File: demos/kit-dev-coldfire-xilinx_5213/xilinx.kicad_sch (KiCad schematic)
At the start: 21 parts, among them P301 CONN_6, P302 CONN_2X2, P303 CONN_20X2, U301 XCR3256-TQ144

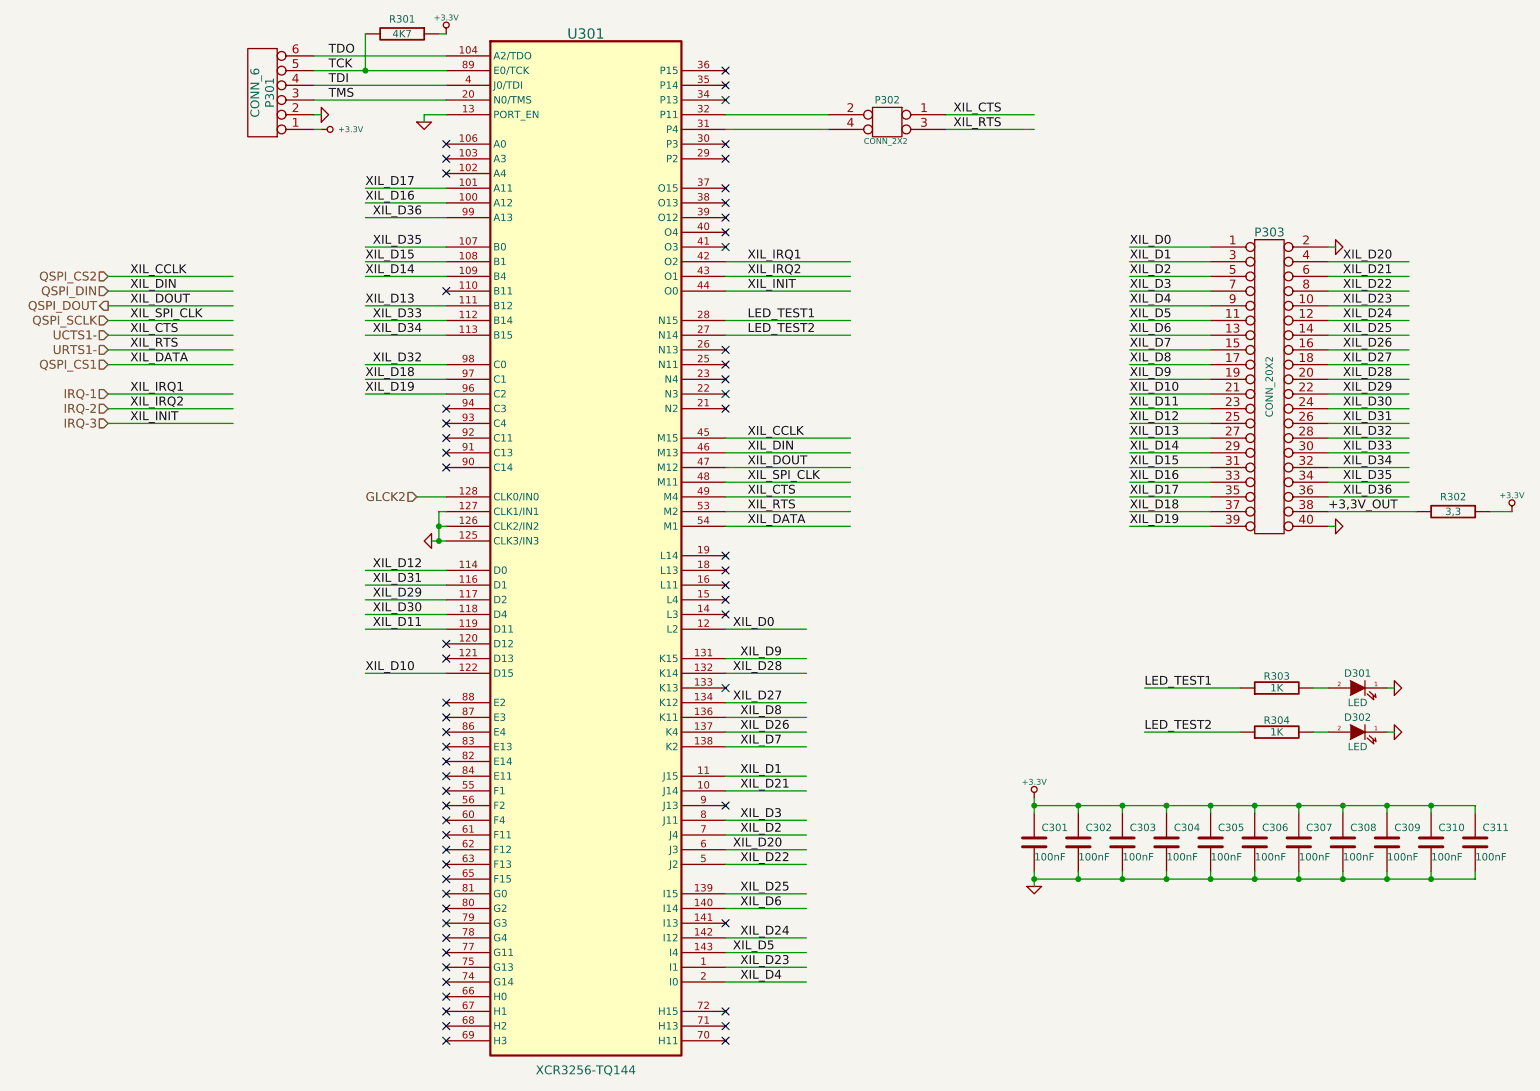
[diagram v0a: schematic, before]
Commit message: feat: update kicad to 9.0.0+dfsg-1
Signed-off-by: lhdjply <lhdjply@126.com>
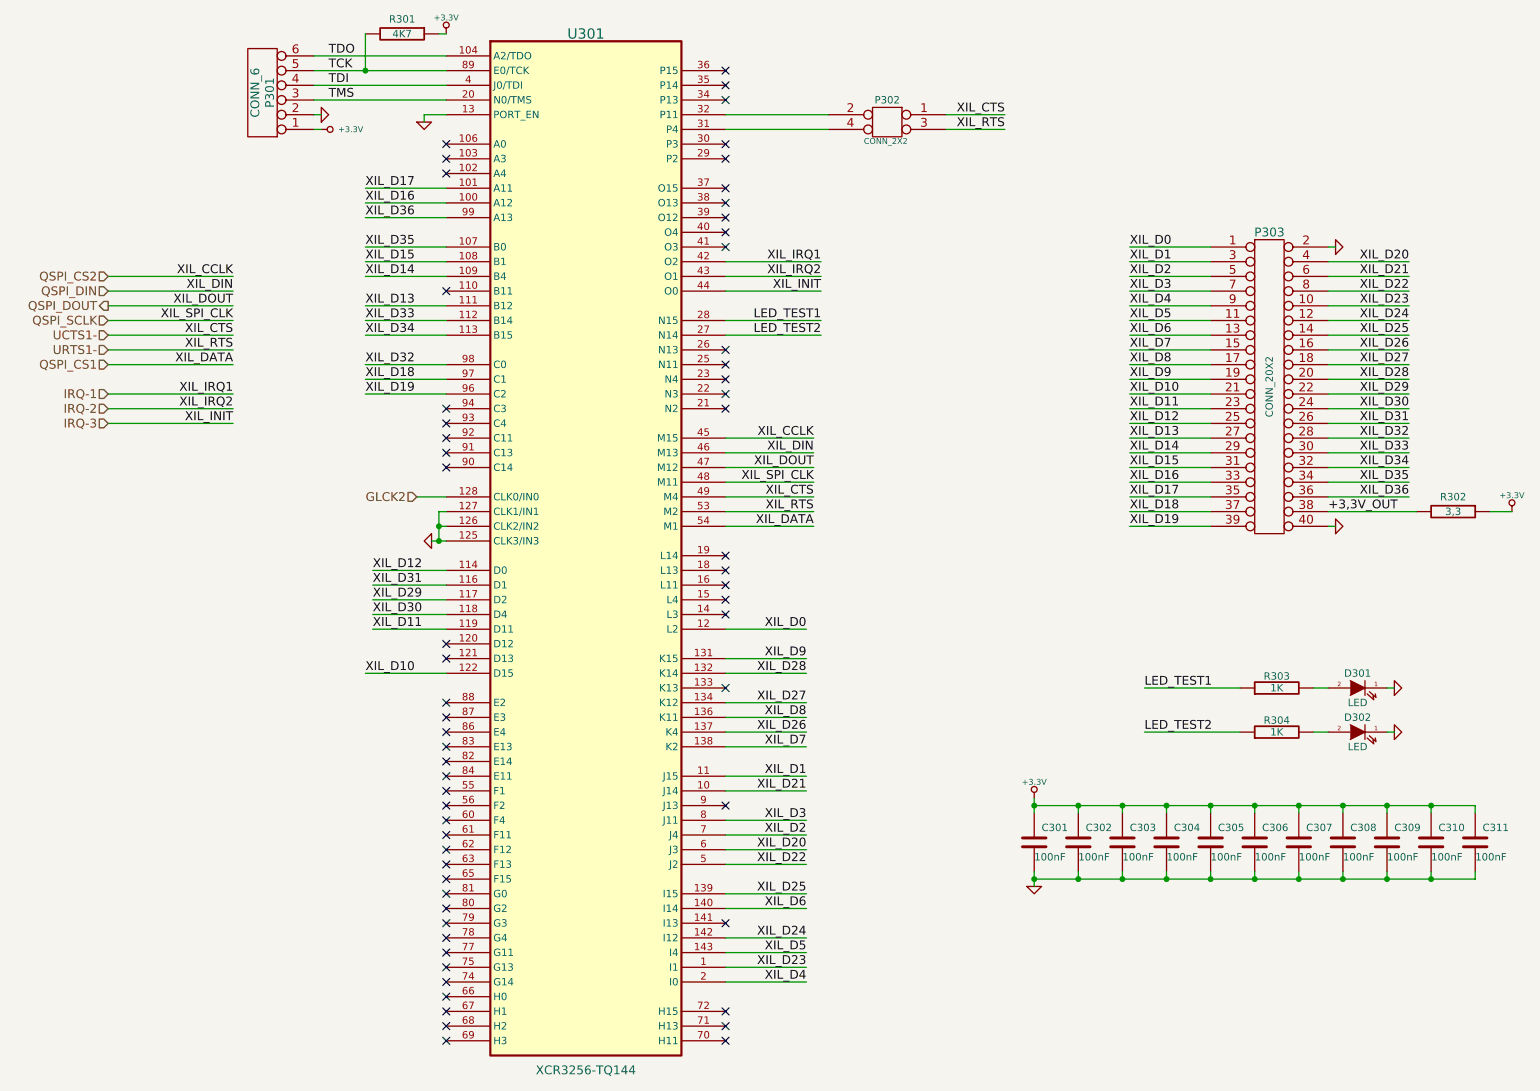
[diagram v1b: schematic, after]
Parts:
- C301, C302, C303, C304, C305, C306, C307, C308, C309, C310, C311: symbol kit-coldfire_schlib:C -> kit-dev-coldfire-xilinx_5213:C
- D301, D302: symbol kit-coldfire_schlib:LED -> kit-dev-coldfire-xilinx_5213:LED
- P301: symbol kit-coldfire_schlib:CONN_6 -> kit-dev-coldfire-xilinx_5213:CONN_6
- P302: symbol kit-coldfire_schlib:CONN_2X2 -> kit-dev-coldfire-xilinx_5213:CONN_2X2
- P303: symbol kit-coldfire_schlib:CONN_20X2 -> kit-dev-coldfire-xilinx_5213:CONN_20X2
- R301, R302, R303, R304: symbol kit-coldfire_schlib:R -> kit-dev-coldfire-xilinx_5213:R
- U301: symbol kit-coldfire_schlib:XCR3256-TQ144 -> kit-dev-coldfire-xilinx_5213:XCR3256-TQ144
